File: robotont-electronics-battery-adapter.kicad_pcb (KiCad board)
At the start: 2 copper layers, 23.5 x 15 mm, 2 parts, among them J1 70AAJ-6-M0G, J2 Conn_01x06

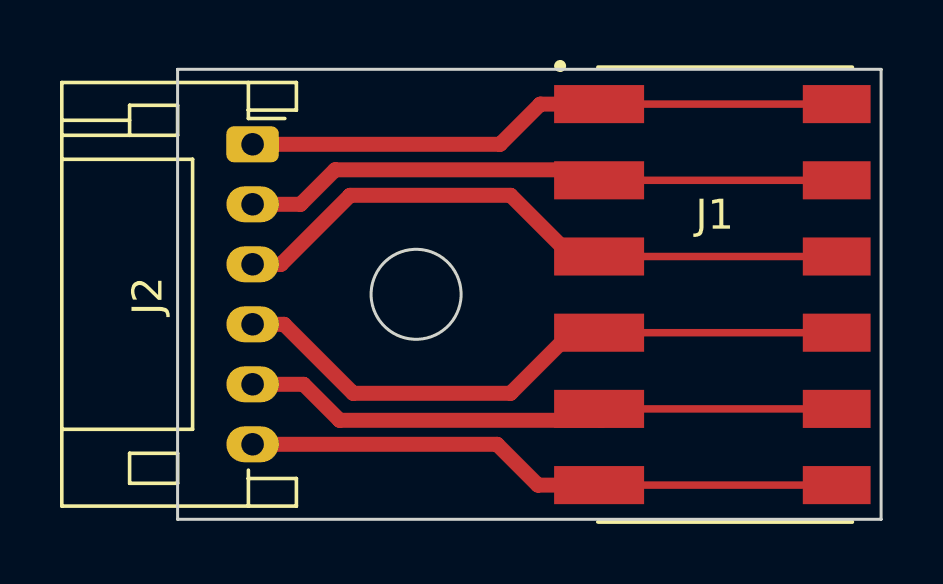
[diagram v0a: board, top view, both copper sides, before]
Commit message: updated to kicad7; replaced jst footprint with pinheader for a cleaner silk;
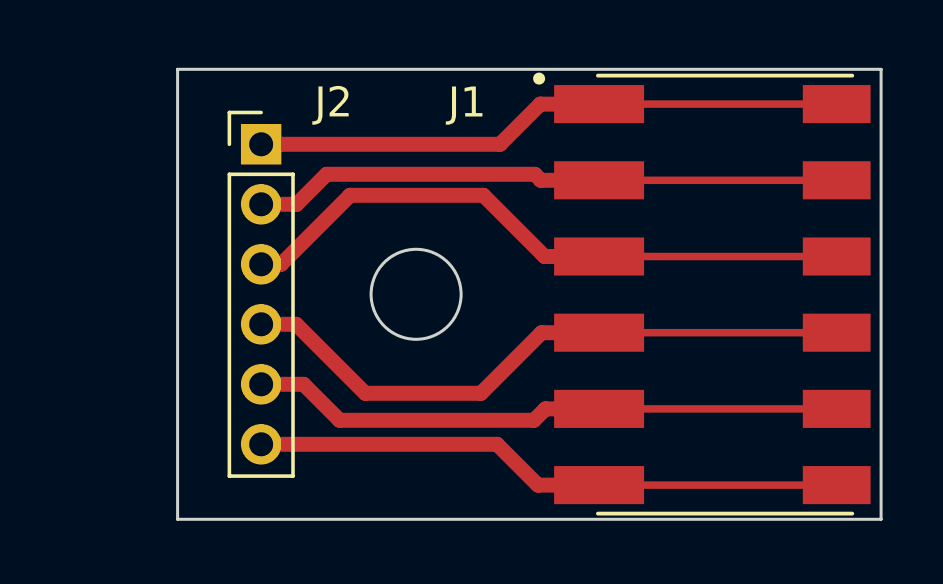
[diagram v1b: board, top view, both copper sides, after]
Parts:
- J2: footprint Connector_JST:JST_PH_S6B-PH-K_1x06_P2.00mm_Horizontal -> Connector_PinHeader_2.00mm:PinHeader_1x06_P2.00mm_Vertical
- moved J2 0.29 mm to (65.8, 54.4), turned to 0 degrees
